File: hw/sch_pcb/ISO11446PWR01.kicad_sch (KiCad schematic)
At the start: 17 parts, among them J1 HEADER_2x04_PARALLEL, J2 HEADER_2x04_PARALLEL, J3 HEADER_2x04_PARALLEL, J4 Conn_01x01_Female, J5 Conn_01x01_Female, J6 Conn_01x01_Female, J7 Conn_01x01_Female, J8 Umin ... Umax, M1 HOLE M3, M2 HOLE M3, M3 HOLE, M4 HOLE

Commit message: An initial test implementation. Both Schema and PCB needs check.
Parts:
- added D1, D2, D3, D4, D5, D6, D7, D8, D9: LED, Mlab_D:LED_1206, symbol Device:LED
- added F1, F4: Polyfuse, Mlab_F:1812, symbol Device:Polyfuse
- added J10: 10 - Spínané 12V +, Mlab_CON:WAGO256, symbol Connector:Conn_01x01_Female
- added J11: 11 - Spínané 12V -, Mlab_CON:WAGO256, symbol Connector:Conn_01x01_Female
- added J12: 12 - Not used, Mlab_CON:WAGO256, symbol Connector:Conn_01x01_Female
- added J13, J16: 13 - Trvalé 12V -, Mlab_CON:WAGO256, symbol Connector:Conn_01x01_Female
- added J15: 13 - Trvalé 12V +, Mlab_CON:WAGO256, symbol Connector:Conn_01x01_Female
- added J17: 13 - Spínané 12V +, Mlab_CON:WAGO256, symbol Connector:Conn_01x01_Female
- added J18: 13 - Spínané 12V -, Mlab_CON:WAGO256, symbol Connector:Conn_01x01_Female
- added J21: Signal Světel, Mlab_Pin_Headers:Straight_2x07, symbol MLAB_HEADER:HEADER_2x07_PARALLEL
- added J5: 5 - Obrsové P, Mlab_CON:WAGO256, symbol Connector:Conn_01x01_Female
- added J6: 6 - Brzdové, Mlab_CON:WAGO256, symbol Connector:Conn_01x01_Female
- added J7: 7 - Obrysové L, Mlab_CON:WAGO256, symbol Connector:Conn_01x01_Female
- added J8: 8 - Couvací, Mlab_CON:WAGO256, symbol Connector:Conn_01x01_Female
- added J9: 9 - Trvalé 12V +, Mlab_CON:WAGO256, symbol Connector:Conn_01x01_Female
- added R1, R12: 800, Mlab_R:SMD-0805, symbol Device:R
- added R10, R11, R13, R14, R15, R16, R17, R18, R19, R20, R21, R22, R23, R9: 240, Mlab_R:SMD-0805, symbol Device:R
- added R2, R3, R4, R5, R6, R7, R8: 36, Mlab_R:R_Axial_Power_L22.0mm_W9.5mm_P30.48mm, symbol Device:R
- added U1, U2, U3, U4, U5, U6, U7: LTV-357T, Package_SO:SO-4_4.4x3.6mm_P2.54mm, symbol Isolator:LTV-357T
- C1: footprint Capacitor_SMD:C_0805_2012Metric -> Mlab_C:SMD-0805
- F2: renamed from F1; footprint Fuse:Fuse_Bourns_MF-RG400 -> Fuse:Fuseholder_Keystone_3555-2
- F3: renamed from F2; footprint Fuse:Fuse_Bourns_MF-RG400 -> Mlab_F:1812
- J1: renamed from J4; value Conn_01x01_Female -> 1 - Směrové L
- J14: renamed from J3; value HEADER_2x04_PARALLEL -> Trvalé 12V
- J19: renamed from J1; value HEADER_2x04_PARALLEL -> Ventilator 12V
- J2: renamed from J5; value Conn_01x01_Female -> 2 - Zadní mlhové
- J20: renamed from J2; value HEADER_2x04_PARALLEL -> Spinane 12V
- J22: renamed from J8; value Umin ... Umax -> Umin ... 5V
- J3: renamed from J6; value Conn_01x01_Female -> 3 - Kostra světla
- J4: renamed from J7; value Conn_01x01_Female -> 4 - Směrové P
- renumbered D1 to D10
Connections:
- net +5V: now also R13.1, R14.1, R15.1, R19.1, R20.1, R21.1, R23.1
- net GND: now also U1.3, U2.3, U3.3, U4.3, U5.3, U6.3, U7.3
- net at J19.3, J19.4: now also F3.2, J19.5, J19.6; no longer J3.1 (Pin_1)
- net S12-: now reaches J20.1, J20.2
- net S12-: now also J19.1, J19.2, J19.7, J19.8, J20.7, J20.8, D2.1 (K), J11.1 (Pin_1), J18.1 (Pin_1)
- net at J20.3, J20.4: now also J20.5, J20.6, F4.2
- net at F2.2: now also J15.1 (Pin_1), R1.1; no longer J1.1 (Pin_1)
- net U12-: now reaches J14.1, J14.2
- net U12-: now also J14.7, J14.8, D1.1 (K), J13.1 (Pin_1), J16.1 (Pin_1)
- net at J14.3, J14.4: now also J14.5, J14.6, F1.2
- net L2: now reaches J2.1 (Pin_1)
- net L2: now also D6.2 (A), R3.1; no longer F3.2
- new net: D4.1 (K), R10.1
- new net: R10.2, U2.1
- new net: D7.1 (K), R17.1
- new net: R17.2, U5.1
- new net: D8.1 (K), R18.1
- new net: R16.2, U4.1
- new net: D6.1 (K), R16.1
- new net: D9.1 (K), R22.1
- new net: R22.2, U7.1
- new net: D3.1 (K), R9.1
- new net: D1.2 (A), R1.2
- new net: D2.2 (A), R12.2
- new net: R18.2, U6.1
- new net: R11.2, U3.1
- new net: D5.1 (K), R11.1
- new net: R9.2, U1.1
- new net L1: D5.2 (A), J1.1 (Pin_1), R2.1
- new net L1S: J21.1, J21.2, R15.2, U3.4
- new net L2S: J21.3, J21.4, R19.2, U4.4
- new net L4: D3.2 (A), J4.1 (Pin_1), R4.1
- new net L4S: J21.5, J21.6, R13.2, U1.4
- new net L5: D7.2 (A), J5.1 (Pin_1), R5.1
- new net L5S: J21.7, J21.8, R20.2, U5.4
- new net L6: D4.2 (A), J6.1 (Pin_1), R6.1
- new net L6S: J21.10, J21.9, R14.2, U2.4
- new net L7: D8.2 (A), J7.1 (Pin_1), R7.1
- new net L7S: J21.11, J21.12, R21.2, U6.4
- new net L8: D9.2 (A), J8.1 (Pin_1), R8.1
- new net L8S: J21.13, J21.14, R23.2, U7.4
- new net L_GND: J3.1 (Pin_1), R2.2, R3.2, R4.2, R5.2, R6.2, R7.2, R8.2, U1.2, U2.2, U3.2, U4.2, U5.2, U6.2, U7.2
- new net S12+: F3.1, F4.1, J10.1 (Pin_1), J17.1 (Pin_1), R12.1
- new net U12+: F1.1, F2.1, J9.1 (Pin_1)
- no-connect marks 5 -> 1
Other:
- note removed: "Delete if unused."
- note removed: "Generally a load module has mounting holes connected to the ground."
- note removed: "Power source modules has mountig holes floating to avoid ground loops."
- note removed: "check if the mounting holles should be connected to ground or not."
- moved on the sheet: F2, F3, J1, J14, J19, J2, J20, J3, J4, M1, M2, M3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

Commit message: drobne upravy schematu
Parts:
- added F5: Fuse, Fuse:Fuseholder_Keystone_3555-2, symbol Device:Fuse
- F1, F3, F4: value Polyfuse -> SD110-16
- J22: value Umin ... 5V -> 5V
- R1, R12: value 800 -> 800R
- R10, R11, R16, R17, R18, R22, R9: value 240 -> 510R
- R13, R14, R15, R19, R20, R21, R23: value 240 -> 2k
- R2, R3, R4, R5, R6, R7, R8: value 36 -> 36R
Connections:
- net S12+: now also F5.2; no longer J17.1 (Pin_1), R12.1
- new net: F5.1, J17.1 (Pin_1), R12.1
- now unconnected: M1.1, M2.1, M3.1, M4.1
- no-connect marks 1 -> 5

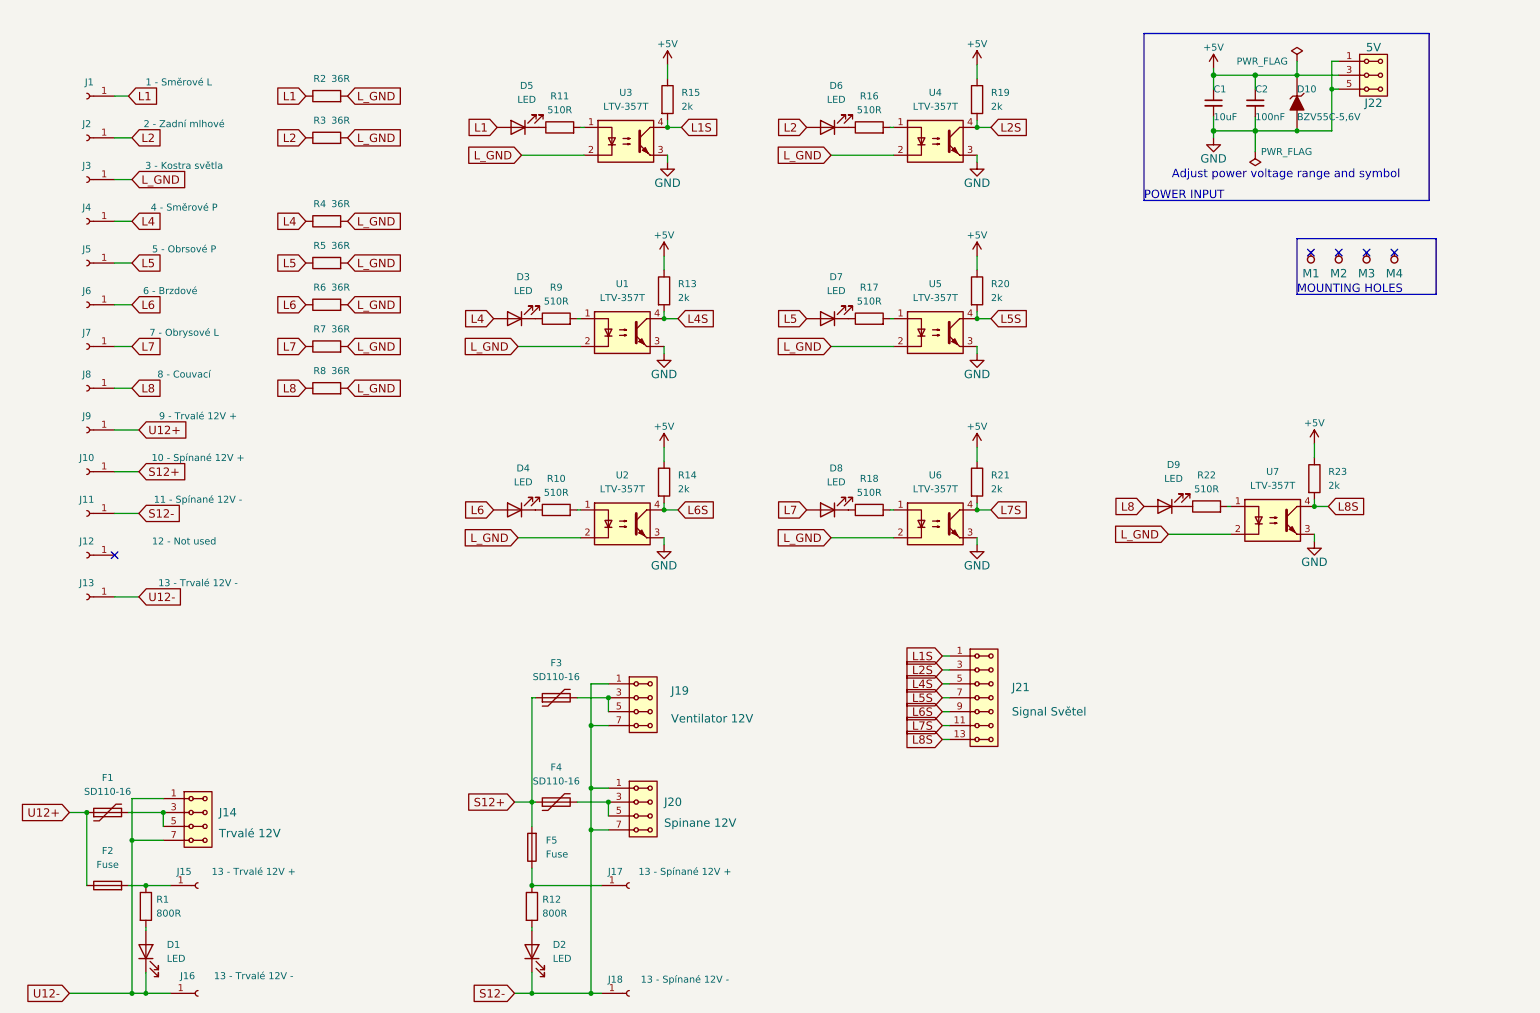
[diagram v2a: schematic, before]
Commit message: Significant schematic and layout improvement. Fixed fuse footprint Fixed schematics   * Spliting to multiple sheets   * Texts translated from czech to english
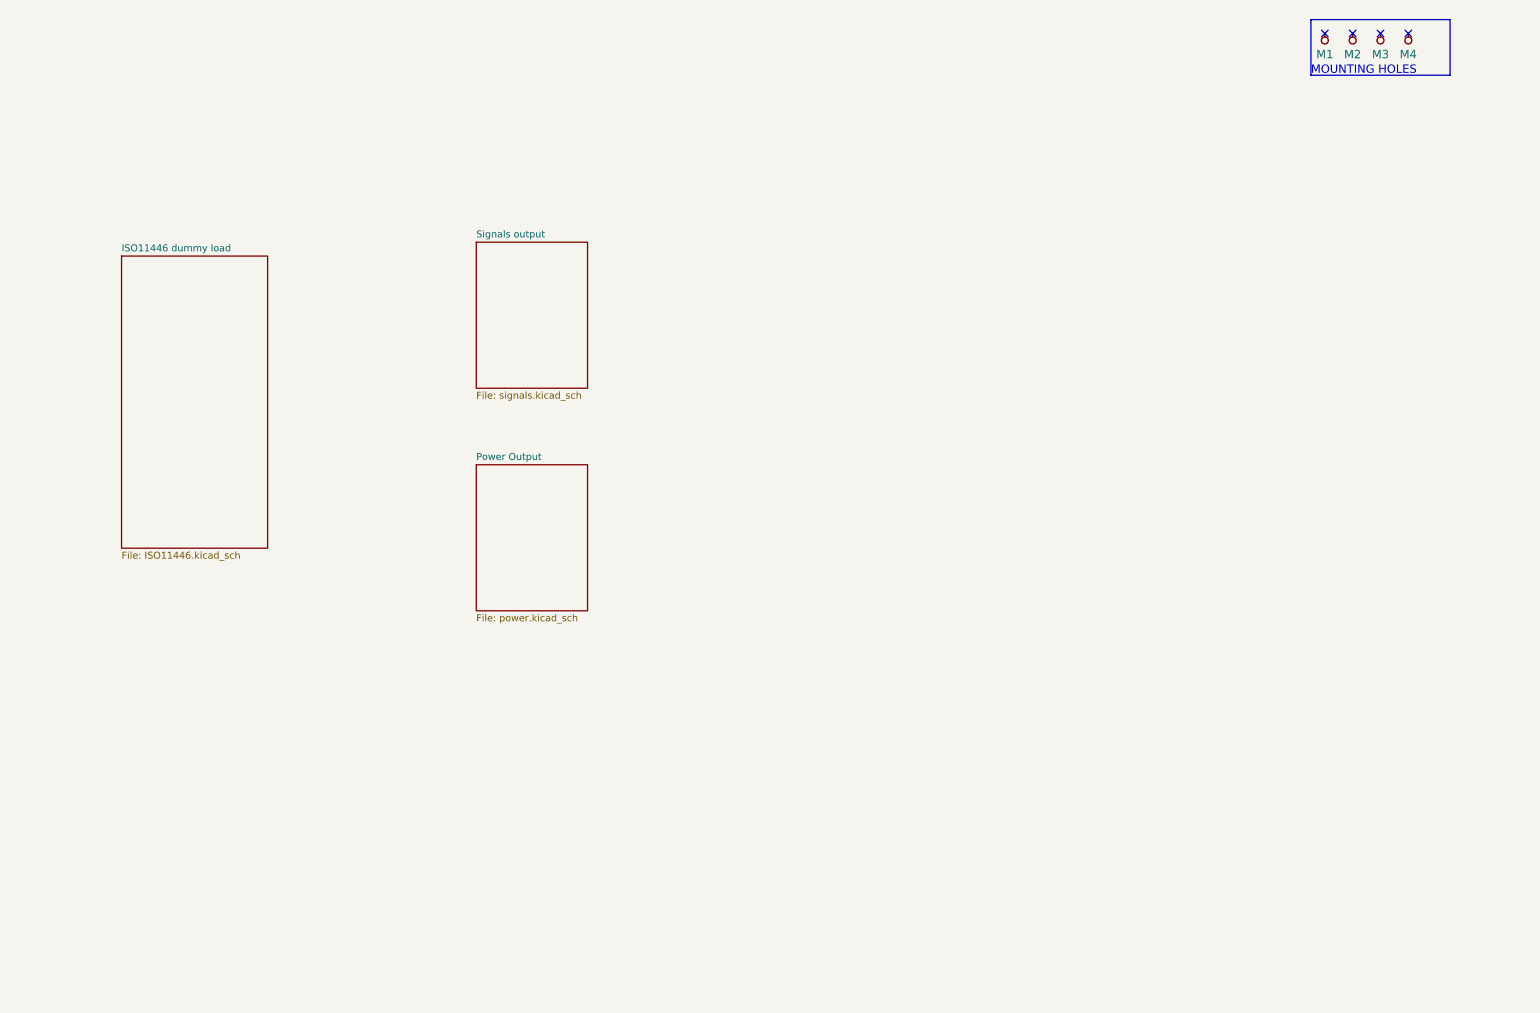
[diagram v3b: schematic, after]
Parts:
- removed C1: 10uF, Mlab_C:SMD-0805, symbol ISM02A-rescue:C_Small-Device-ISM02A-rescue
- removed C2: 100nF, Capacitor_SMD:C_0805_2012Metric, symbol ISM02A-rescue:C_Small-Device-ISM02A-rescue
- removed D1, D2, D3, D4, D5, D6, D7, D8, D9: LED, Mlab_D:LED_1206, symbol Device:LED
- removed D10: BZV55C-5,6V, Diode_SMD:D_SMA, symbol ISM02A-rescue:D_ZENER-MLAB_D
- removed F1, F3, F4: SD110-16, Mlab_F:1812, symbol Device:Polyfuse
- removed F2, F5: Fuse, Fuse:Fuseholder_Keystone_3555-2, symbol Device:Fuse
- removed J1: 1 - Směrové L, Mlab_CON:WAGO256, symbol Connector:Conn_01x01_Female
- removed J10: 10 - Spínané 12V +, Mlab_CON:WAGO256, symbol Connector:Conn_01x01_Female
- removed J11: 11 - Spínané 12V -, Mlab_CON:WAGO256, symbol Connector:Conn_01x01_Female
- removed J12: 12 - Not used, Mlab_CON:WAGO256, symbol Connector:Conn_01x01_Female
- removed J13, J16: 13 - Trvalé 12V -, Mlab_CON:WAGO256, symbol Connector:Conn_01x01_Female
- removed J14: Trvalé 12V, Mlab_Pin_Headers:Straight_2x04, symbol MLAB_HEADER:HEADER_2x04_PARALLEL
- removed J15: 13 - Trvalé 12V +, Mlab_CON:WAGO256, symbol Connector:Conn_01x01_Female
- removed J17: 13 - Spínané 12V +, Mlab_CON:WAGO256, symbol Connector:Conn_01x01_Female
- removed J18: 13 - Spínané 12V -, Mlab_CON:WAGO256, symbol Connector:Conn_01x01_Female
- removed J19: Ventilator 12V, Mlab_Pin_Headers:Straight_2x04, symbol MLAB_HEADER:HEADER_2x04_PARALLEL
- removed J2: 2 - Zadní mlhové, Mlab_CON:WAGO256, symbol Connector:Conn_01x01_Female
- removed J20: Spinane 12V, Mlab_Pin_Headers:Straight_2x04, symbol MLAB_HEADER:HEADER_2x04_PARALLEL
- removed J21: Signal Světel, Mlab_Pin_Headers:Straight_2x07, symbol MLAB_HEADER:HEADER_2x07_PARALLEL
- removed J22: 5V, Mlab_Pin_Headers:Straight_2x03, symbol header:HEADER_2x03_PARALLEL
- removed J3: 3 - Kostra světla, Mlab_CON:WAGO256, symbol Connector:Conn_01x01_Female
- removed J4: 4 - Směrové P, Mlab_CON:WAGO256, symbol Connector:Conn_01x01_Female
- removed J5: 5 - Obrsové P, Mlab_CON:WAGO256, symbol Connector:Conn_01x01_Female
- removed J6: 6 - Brzdové, Mlab_CON:WAGO256, symbol Connector:Conn_01x01_Female
- removed J7: 7 - Obrysové L, Mlab_CON:WAGO256, symbol Connector:Conn_01x01_Female
- removed J8: 8 - Couvací, Mlab_CON:WAGO256, symbol Connector:Conn_01x01_Female
- removed J9: 9 - Trvalé 12V +, Mlab_CON:WAGO256, symbol Connector:Conn_01x01_Female
- removed R1, R12: 800R, Mlab_R:SMD-0805, symbol Device:R
- removed R10, R11, R16, R17, R18, R22, R9: 510R, Mlab_R:SMD-0805, symbol Device:R
- removed R13, R14, R15, R19, R20, R21, R23: 2k, Mlab_R:SMD-0805, symbol Device:R
- removed R2, R3, R4, R5, R6, R7, R8: 36R, Mlab_R:R_Axial_Power_L22.0mm_W9.5mm_P30.48mm, symbol Device:R
- removed U1, U2, U3, U4, U5, U6, U7: LTV-357T, Package_SO:SO-4_4.4x3.6mm_P2.54mm, symbol Isolator:LTV-357T
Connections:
- no-connect marks 5 -> 4
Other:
- added sheet ISO11446 dummy load (ISO11446.kicad_sch)
- added sheet Power Output (power.kicad_sch)
- added sheet Signals output (signals.kicad_sch)
- note removed: "Adjust power voltage range and symbol"
- note removed: "POWER INPUT"
- moved on the sheet: M1, M2, M3, M4
